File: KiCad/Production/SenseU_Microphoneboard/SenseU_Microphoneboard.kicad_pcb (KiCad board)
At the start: 2 copper layers, 20 parts, among them J1 90122-0126

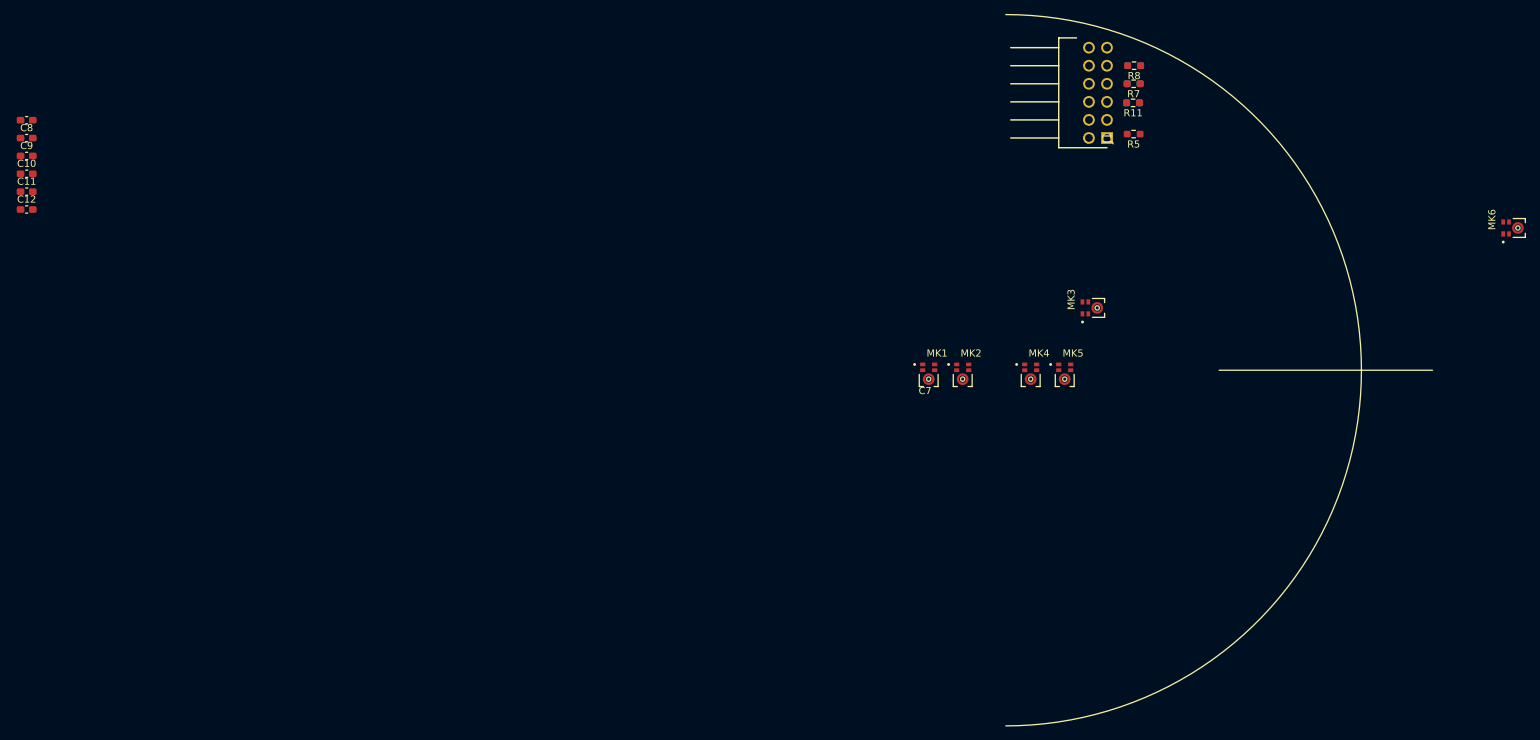
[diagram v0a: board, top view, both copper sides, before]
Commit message: PCB V1 finished (9 MEMS), DRC violation rules pending
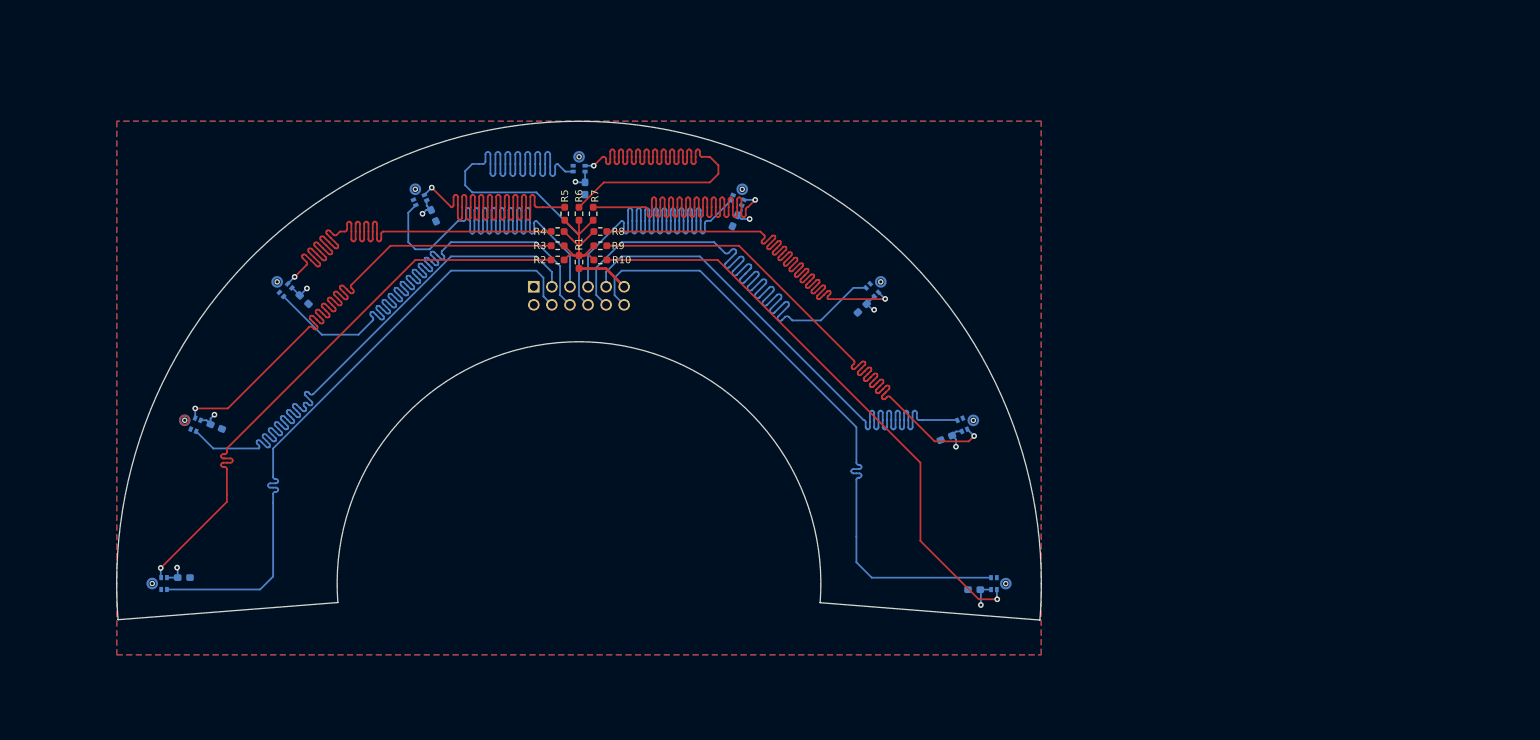
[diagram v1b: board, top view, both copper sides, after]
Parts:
- removed R11: 0, Resistor_SMD:R_0603_1608Metric_Pad0.98x0.95mm_HandSolder
- added C7: 0.1uF, Capacitor_SMD:C_0603_1608Metric_Pad1.08x0.95mm_HandSolder, B.Cu at (139.8, 81.3)
- added C8: 0.1uF, Capacitor_SMD:C_0603_1608Metric_Pad1.08x0.95mm_HandSolder, B.Cu at (151.7, 99.5)
- added C9: 0.1uF, Capacitor_SMD:C_0603_1608Metric_Pad1.08x0.95mm_HandSolder, B.Cu at (155.6, 120.8)
- added MK7: SPH0655LM4H-1, SenseU_Microphoneboard:MIC_SPH0655LM4H-1, B.Cu at (141.9, 78.1)
- added MK8: SPH0655LM4H-1, SenseU_Microphoneboard:MIC_SPH0655LM4H-1, B.Cu at (154.8, 97.3)
- added MK9: SPH0655LM4H-1, SenseU_Microphoneboard:MIC_SPH0655LM4H-1, B.Cu at (159.3, 120.0)
- added R1: 51, Resistor_SMD:R_0603_1608Metric_Pad0.98x0.95mm_HandSolder, F.Cu at (100.0, 74.8)
- added R2: 0, Resistor_SMD:R_0603_1608Metric_Pad0.98x0.95mm_HandSolder, F.Cu at (97.0, 74.5)
- added R3: 0, Resistor_SMD:R_0603_1608Metric_Pad0.98x0.95mm_HandSolder, F.Cu at (97.0, 72.5)
- added R4: 0, Resistor_SMD:R_0603_1608Metric_Pad0.98x0.95mm_HandSolder, F.Cu at (97.0, 70.5)
- C1: renamed from C7; moved to B.Cu
- C2: renamed from C8; moved to B.Cu
- C3: renamed from C9; moved to B.Cu
- C4: renamed from C10; moved to B.Cu
- C5: renamed from C11; moved to B.Cu
- C6: renamed from C12; moved to B.Cu
- J1, MK1, MK2, MK3, MK4, MK5, MK6: moved to B.Cu
- R10, R6, R9: moved to F.Cu
- R5: value 51 -> 0
- moved MK3 114.1 mm to (58.1, 78.1), turned to 45.875 degrees
- moved MK1 112.4 mm to (40.7, 120.0), turned to 90 degrees
- moved MK2 108.9 mm to (45.2, 97.3), turned to 67.937 degrees
- moved MK6 108.7 mm to (122.7, 65.2), turned to -23.814 degrees
- moved C6 99.6 mm to (121.9, 69.0), turned to -113.814 degrees
- moved MK4 89.9 mm to (77.3, 65.2), turned to 23.814 degrees
- moved J1 83.3 mm to (93.7, 78.3), turned to 0 degrees
- moved R5 80.8 mm to (98.0, 68.0), turned to 90 degrees
- moved R6 79.4 mm to (100.0, 68.0), turned to 90 degrees
- moved R9 79.2 mm to (103.0, 72.5), turned to 0 degrees
- moved R10 79.0 mm to (103.0, 74.5), turned to 0 degrees
- moved R8 78.6 mm to (103.0, 70.5), turned to 0 degrees
- moved C5 78.5 mm to (100.8, 64.5), turned to -90 degrees
- moved R7 78.2 mm to (102.0, 68.0), turned to 90 degrees
- moved MK5 74.5 mm to (100.0, 60.7)
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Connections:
- J1 pad 10: Net-(J1-D6) -> PDM-7
- J1 pad 11: unconnected-(J1-D7-Pad11) -> Net-(J1-CLK)
- J1 pad 12: unconnected-(J1-D8-Pad12) -> PDM-9
- J1 pad 3: unconnected-(J1-/-Pad3) -> PDM-2
- J1 pad 4: Net-(J1-CLK) -> PDM-1
- J1 pad 5: Net-(J1-D1) -> PDM-4
- J1 pad 6: Net-(J1-D2) -> PDM-3
- J1 pad 7: Net-(J1-D3) -> PDM-6
- J1 pad 8: Net-(J1-D4) -> PDM-5
- J1 pad 9: Net-(J1-D5) -> PDM-8
- MK1 pad 4: CLK -> CLK-1
- MK2 pad 4: CLK -> CLK-2
- MK3 pad 4: CLK -> CLK-3
- MK4 pad 1: PDM-6 -> PDM-4
- MK4 pad 4: CLK -> CLK-4
- MK5 pad 1: PDM-4 -> PDM-5
- MK5 pad 4: CLK -> CLK-5
- MK6 pad 1: PDM-5 -> PDM-6
- MK6 pad 4: CLK -> CLK-6
- R10 pad 1: PDM-3 -> CLK
- R10 pad 2: Net-(J1-D3) -> CLK-9
- R5 pad 2: Net-(J1-CLK) -> CLK-4
- R6 pad 1: PDM-2 -> CLK
- R6 pad 2: Net-(J1-D2) -> CLK-5
- R7 pad 1: PDM-4 -> CLK
- R7 pad 2: Net-(J1-D4) -> CLK-6
- R8 pad 1: PDM-6 -> CLK
- R8 pad 2: Net-(J1-D6) -> CLK-7
- R9 pad 1: PDM-5 -> CLK
- R9 pad 2: Net-(J1-D5) -> CLK-8
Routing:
- net PDM-9: track 0.00 -> 89.9 mm
- net PDM-1: track 0.00 -> 89.9 mm
- net PDM-8: track 0.00 -> 89.7 mm
- net PDM-4: track 0.00 -> 89.6 mm
- net PDM-5: track 0.00 -> 89.6 mm
- net PDM-2: track 0.00 -> 89.6 mm
- net PDM-6: track 0.00 -> 89.5 mm
- net PDM-7: track 0.00 -> 89.5 mm
- net PDM-3: track 0.00 -> 89.4 mm
- net CLK-9: track 0.00 -> 82.5 mm, vias 0 -> 1
- net CLK-1: track 0.00 -> 82.4 mm, vias 0 -> 1
- net CLK-8: track 0.00 -> 82.2 mm, vias 0 -> 1
- net CLK-2: track 0.00 -> 82.1 mm, vias 0 -> 1
- net CLK-3: track 0.00 -> 82.0 mm, vias 0 -> 1
- net CLK-4: track 0.00 -> 82.0 mm, vias 0 -> 1
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- added copper zone on F.Cu, net 3.3V
- added copper zone on B.Cu, net GND
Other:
- board outline added: 130 x 70.1 mm
